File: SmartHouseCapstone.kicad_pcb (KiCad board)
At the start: 2 copper layers, 100.5 x 107.4 mm, 68 parts, among them J1 5V In, J2 3v3 In, J3 1602 LCD, J4 Stepper Motor Terminal, J5 Physical Switch Terminal, J6 MOSFET Switch Module Terminal, J7 Fingerprint Scanner Terminal, J8 Servo Terminal, J9 RFID Module Terminal, Q1 FDN340P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

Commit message: revision 1
added pull-down resistor to FDN430P MosFET Gate

revised pcb layout
revised schematic layout

generated new BOM
generated new Backup
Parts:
- added R27: 2.2k, Resistor_THT:R_Axial_DIN0207_L6.3mm_D2.5mm_P7.62mm_Horizontal, F.Cu at (134.0, 112.0)
- R25: value 47 -> 100
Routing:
- net /Security System/servo_switch: track 61.5 -> 69.6 mm
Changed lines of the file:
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@@
 	)
 	(paper "A4")
+	(title_block
+		(title "Smart House Control Board")
+		(date "2025-11-03")
+		(rev "1")
+	)
 	(layers
 		(0 "F.Cu" signal)
@@
 			)
 		)
-		(property "Value" "47"
+		(property "Value" "100"
 			(at -3.015 0 0)
 			(layer "F.Fab")
@@
 	(footprint "Resistor_THT:R_Axial_DIN0207_L6.3mm_D2.5mm_P7.62mm_Horizontal"
 		(layer "F.Cu")
+		(at 134 112 90)
+		(descr "Resistor, Axial_DIN0207 series, Axial, Horizontal, pin pitch=7.62mm, 0.25W = 1/4W, length*diameter=6.3*2.5mm^2, http://cdn-reichelt.de/documents/datenblatt/B400/1_4W%23YAG.pdf")
+		(tags "Resistor Axial_DIN0207 series Axial Horizontal pin pitch 7.62mm 0.25W = 1/4W length 6.3mm diameter 2.5mm")
+		(property "Reference" "R27"
+			(at 3.81 -2.37 90)
+			(layer "F.SilkS")
+			(effects
+				(font
+					(size 1 1)
+					(thickness 0.15)
+				)
+			)
+		)
+		(property "Value" "2.2k"
+			(at 3.81 2.37 90)
+			(layer "F.Fab")
+			(effects
+				(font
+					(size 1 1)
+					(thickness 0.15)
+				)
+			)
+		)
+		(property "Datasheet" "~"
+			(at 0 0 90)
+			(layer "F.Fab")
+			(hide yes)
+			(effects
+				(font
+					(size 1.27 1.27)
+					(thickness 0.15)
+				)
+			)
+		)
+		(property "Description" "Resistor"
+			(at 0 0 90)
+			(layer "F.Fab")
+			(hide yes)
+			(effects
+				(font
+					(size 1.27 1.27)
+					(thickness 0.15)
+				)
+			)
+		)
+		(property ki_fp_filters "R_*")
+		(sheetname "/Security System/")
+		(sheetfile "SecuritySystem.kicad_sch")
+		(attr through_hole)
+		(fp_line
+			(start 7.08 -1.37)
+			(end 7.08 -1.04)
+			(stroke
+				(width 0.12)
+				(type solid)
+			)
+			(layer "F.SilkS")
+		)
+		(fp_line
+			(start 0.54 -1.37)
+			(end 7.08 -1.37)
+			(stroke
+				(width 0.12)
+				(type solid)
+			)
+			(layer "F.SilkS")
+		)
+		(fp_line
+			(start 0.54 -1.04)
+			(end 0.54 -1.37)
+			(stroke
+				(width 0.12)
+				(type solid)
+			)
+			(layer "F.SilkS")
+		)
+		(fp_line
+			(start 0.54 1.04)
+			(end 0.54 1.37)
+			(stroke
+				(width 0.12)
+				(type solid)
+			)
+			(layer "F.SilkS")
+		)
+		(fp_line
+			(start 7.08 1.37)
+			(end 7.08 1.04)
+			(stroke
+				(width 0.12)
+				(type solid)
+			)
+			(layer "F.SilkS")
+		)
+		(fp_line
+			(start 0.54 1.37)
+			(end 7.08 1.37)
+			(stroke
+				(width 0.12)
+				(type solid)
+			)
+			(layer "F.SilkS")
+		)
+		(fp_rect
+			(start -1.05 -1.5)
+			(end 8.67 1.5)
+			(stroke
+				(width 0.05)
+				(type solid)
+			)
+			(fill no)
+			(layer "F.CrtYd")
+		)
+		(fp_line
+			(start 7.62 0)
+			(end 6.96 0)
+			(stroke
+				(width 0.1)
+				(type solid)
+			)
+			(layer "F.Fab")
+		)
+		(fp_line
+			(start 0 0)
+			(end 0.66 0)
+			(stroke
+				(width 0.1)
+				(type solid)
+			)
+			(layer "F.Fab")
+		)
+		(fp_rect
+			(start 0.66 -1.25)
+			(end 6.96 1.25)
+			(stroke
+				(width 0.1)
+				(type solid)
+			)
+			(fill no)
+			(layer "F.Fab")
+		)
+		(fp_text user "${REFERENCE}"
+			(at 3.81 0 90)
+			(layer "F.Fab")
+			(effects
+				(font
+					(size 1 1)
+					(thickness 0.15)
+				)
+			)
+		)
+		(pad "1" thru_hole circle
+			(at 0 0 90)
+			(size 1.6 1.6)
+			(drill 0.8)
+			(layers "*.Cu" "*.Mask")
+			(remove_unused_layers no)
+			(net 60 "/Security System/servo_switch")
+			(pintype "passive")
+		)
+		(pad "2" thru_hole circle
+			(at 7.62 0 90)
+			(size 1.6 1.6)
+			(drill 0.8)
+			(layers "*.Cu" "*.Mask")
+			(remove_unused_layers no)
+			(net 1 "GND")
+			(pintype "passive")
+		)
+		(embedded_fonts no)
+		(model "${KICAD9_3DMODEL_DIR}/Resistor_THT.3dshapes/R_Axial_DIN0207_L6.3mm_D2.5mm_P7.62mm_Horizontal.step"
+			(offset
+				(xyz 0 0 0)
+			)
+			(scale
+				(xyz 1 1 1)
+			)
+			(rotate
+				(xyz 0 0 0)
+			)
+		)
+	)
+	(footprint "Resistor_THT:R_Axial_DIN0207_L6.3mm_D2.5mm_P7.62mm_Horizontal"
+		(layer "F.Cu")
 		(at 83.92 92.3 180)
 		(descr "Resistor, Axial_DIN0207 series, Axial, Horizontal, pin pitch=7.62mm, 0.25W = 1/4W, length*diameter=6.3*2.5mm^2, http://cdn-reichelt.de/documents/datenblatt/B400/1_4W%23YAG.pdf")
@@
 	)
 	(segment
+		(start 134.256 120)
+		(end 134.256 112.256)
+		(width 0.8)
+		(layer "B.Cu")
+		(net 60)
+	)
+	(segment
 		(start 132.59 123.48)
 		(end 134.256 121.814)
@@
 	)
 	(segment
-		(start 134.256 121.814)
+		(start 134.256 112.256)
+		(end 134 112)
+		(width 0.8)
+		(layer "B.Cu")
+		(net 60)
+	)
+	(segment
+		(start 134.256 120)
 		(end 134.256 119.596)
 		(width 0.8)
 		(layer "B.Cu")
+		(net 60)
+	)
+	(segment
+		(start 134.256 121.814)
+		(end 134.256 120)
+		(width 0.8)
+		(layer "B.Cu")

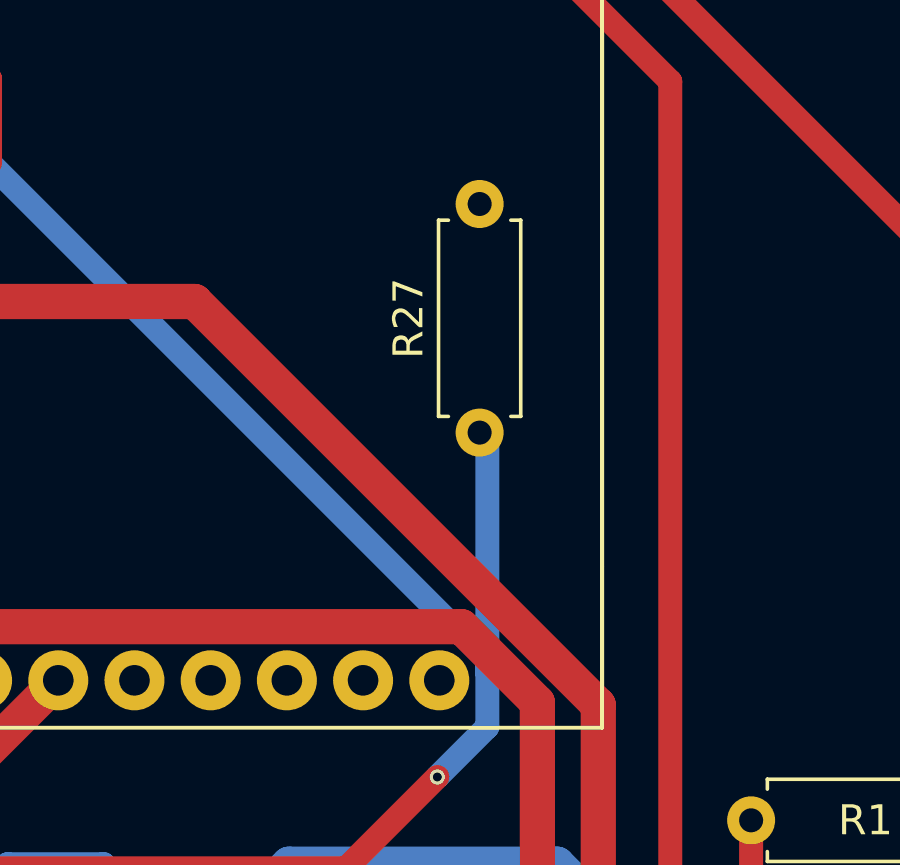
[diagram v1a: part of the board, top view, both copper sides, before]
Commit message: updated gerber files
re-add of resistor footprints -- for some reason it was removed
re-add of the new pull-down resistor R27 -- for some reason it was not
in the schematic but it exists in pcb
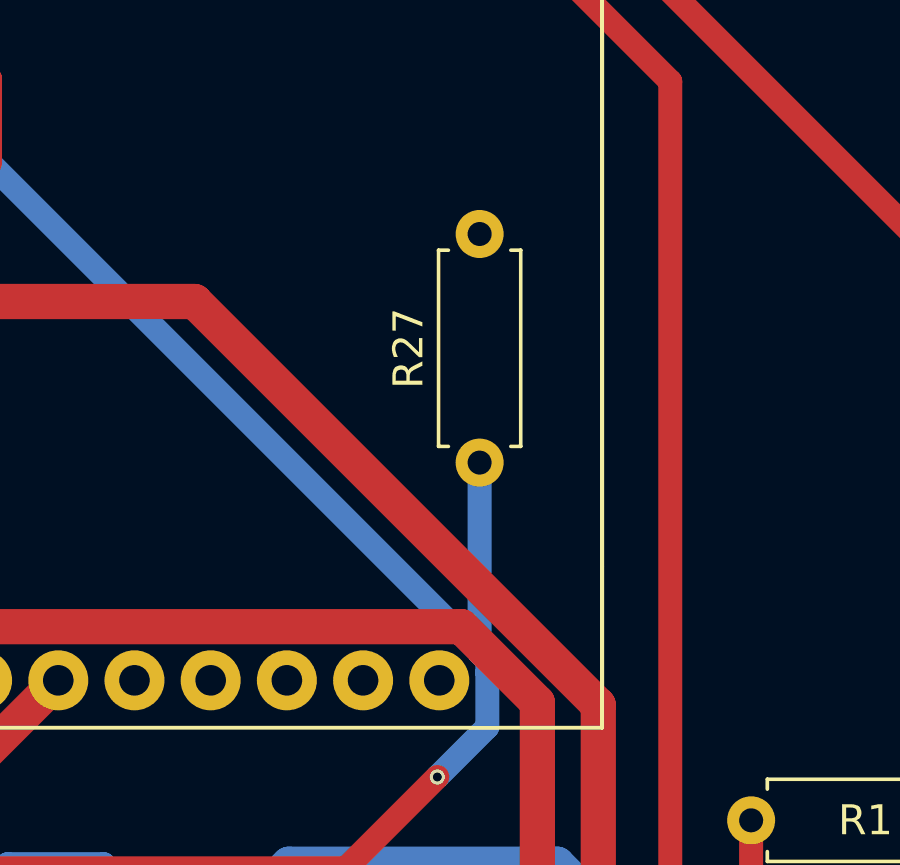
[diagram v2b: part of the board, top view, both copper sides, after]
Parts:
- moved R27 1.00 mm to (134.0, 113.0)
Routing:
- net /Security System/servo_switch: track 69.6 -> 68.2 mm
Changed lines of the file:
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@@
 	(footprint "Resistor_THT:R_Axial_DIN0207_L6.3mm_D2.5mm_P7.62mm_Horizontal"
 		(layer "F.Cu")
+		(at 134 113 90)
+		(descr "Resistor, Axial_DIN0207 series, Axial, Horizontal, pin pitch=7.62mm, 0.25W = 1/4W, length*diameter=6.3*2.5mm^2, http://cdn-reichelt.de/documents/datenblatt/B400/1_4W%23YAG.pdf")
+		(tags "Resistor Axial_DIN0207 series Axial Horizontal pin pitch 7.62mm 0.25W = 1/4W length 6.3mm diameter 2.5mm")
+		(property "Reference" "R27"
+			(at 3.81 -2.37 90)
+			(layer "F.SilkS")
+			(effects
+				(font
+					(size 1 1)
+					(thickness 0.15)
+				)
+			)
+		)
+		(property "Value" "2.2k"
+			(at 3.81 2.37 90)
+			(layer "F.Fab")
+			(effects
+				(font
+					(size 1 1)
+					(thickness 0.15)
+				)
+			)
+		)
+		(property "Datasheet" "~"
+			(at 0 0 90)
+			(layer "F.Fab")
+			(hide yes)
+			(effects
+				(font
+					(size 1.27 1.27)
+					(thickness 0.15)
+				)
+			)
+		)
+		(property "Description" "Resistor"
+			(at 0 0 90)
+			(layer "F.Fab")
+			(hide yes)
+			(effects
+				(font
+					(size 1.27 1.27)
+					(thickness 0.15)
+				)
+			)
+		)
+		(property ki_fp_filters "R_*")
+		(sheetname "/Security System/")
+		(sheetfile "SecuritySystem.kicad_sch")
+		(attr through_hole)
+		(fp_line
+			(start 7.08 -1.37)
+			(end 7.08 -1.04)
+			(stroke
+				(width 0.12)
+				(type solid)
+			)
+			(layer "F.SilkS")
+		)
+		(fp_line
+			(start 0.54 -1.37)
+			(end 7.08 -1.37)
+			(stroke
+				(width 0.12)
+				(type solid)
+			)
+			(layer "F.SilkS")
+		)
+		(fp_line
+			(start 0.54 -1.04)
+			(end 0.54 -1.37)
+			(stroke
+				(width 0.12)
+				(type solid)
+			)
+			(layer "F.SilkS")
+		)
+		(fp_line
+			(start 0.54 1.04)
+			(end 0.54 1.37)
+			(stroke
+				(width 0.12)
+				(type solid)
+			)
+			(layer "F.SilkS")
+		)
+		(fp_line
+			(start 7.08 1.37)
+			(end 7.08 1.04)
+			(stroke
+				(width 0.12)
+				(type solid)
+			)
+			(layer "F.SilkS")
+		)
+		(fp_line
+			(start 0.54 1.37)
+			(end 7.08 1.37)
+			(stroke
+				(width 0.12)
+				(type solid)
+			)
+			(layer "F.SilkS")
+		)
+		(fp_rect
+			(start -1.05 -1.5)
+			(end 8.67 1.5)
+			(stroke
+				(width 0.05)
+				(type solid)
+			)
+			(fill no)
+			(layer "F.CrtYd")
+		)
+		(fp_line
+			(start 7.62 0)
+			(end 6.96 0)
+			(stroke
+				(width 0.1)
+				(type solid)
+			)
+			(layer "F.Fab")
+		)
+		(fp_line
+			(start 0 0)
+			(end 0.66 0)
+			(stroke
+				(width 0.1)
+				(type solid)
+			)
+			(layer "F.Fab")
+		)
+		(fp_rect
+			(start 0.66 -1.25)
+			(end 6.96 1.25)
+			(stroke
+				(width 0.1)
+				(type solid)
+			)
+			(fill no)
+			(layer "F.Fab")
+		)
+		(fp_text user "${REFERENCE}"
+			(at 3.81 0 90)
+			(layer "F.Fab")
+			(effects
+				(font
+					(size 1 1)
+					(thickness 0.15)
+				)
+			)
+		)
+		(pad "1" thru_hole circle
+			(at 0 0 90)
+			(size 1.6 1.6)
+			(drill 0.8)
+			(layers "*.Cu" "*.Mask")
+			(remove_unused_layers no)
+			(net 60 "/Security System/servo_switch")
+			(pintype "passive")
+		)
+		(pad "2" thru_hole circle
+			(at 7.62 0 90)
+			(size 1.6 1.6)
+			(drill 0.8)
+			(layers "*.Cu" "*.Mask")
+			(remove_unused_layers no)
+			(net 1 "GND")
+			(pintype "passive")
+		)
+		(embedded_fonts no)
+		(model "${KICAD9_3DMODEL_DIR}/Resistor_THT.3dshapes/R_Axial_DIN0207_L6.3mm_D2.5mm_P7.62mm_Horizontal.step"
+			(offset
+				(xyz 0 0 0)
+			)
+			(scale
+				(xyz 1 1 1)
+			)
+			(rotate
+				(xyz 0 0 0)
+			)
+		)
+	)
+	(footprint "Resistor_THT:R_Axial_DIN0207_L6.3mm_D2.5mm_P7.62mm_Horizontal"
+		(layer "F.Cu")
 		(at 83.77 114.625 180)
 		(descr "Resistor, Axial_DIN0207 series, Axial, Horizontal, pin pitch=7.62mm, 0.25W = 1/4W, length*diameter=6.3*2.5mm^2, http://cdn-reichelt.de/documents/datenblatt/B400/1_4W%23YAG.pdf")
@@
 	(footprint "Resistor_THT:R_Axial_DIN0207_L6.3mm_D2.5mm_P7.62mm_Horizontal"
 		(layer "F.Cu")
-		(at 134 112 90)
-		(descr "Resistor, Axial_DIN0207 series, Axial, Horizontal, pin pitch=7.62mm, 0.25W = 1/4W, length*diameter=6.3*2.5mm^2, http://cdn-reichelt.de/documents/datenblatt/B400/1_4W%23YAG.pdf")
-		(tags "Resistor Axial_DIN0207 series Axial Horizontal pin pitch 7.62mm 0.25W = 1/4W length 6.3mm diameter 2.5mm")
-		(property "Reference" "R27"
-			(at 3.81 -2.37 90)
-			(layer "F.SilkS")
-			(effects
-				(font
-					(size 1 1)
-					(thickness 0.15)
-				)
-			)
-		)
-		(property "Value" "2.2k"
-			(at 3.81 2.37 90)
-			(layer "F.Fab")
-			(effects
-				(font
-					(size 1 1)
-					(thickness 0.15)
-				)
-			)
-		)
-		(property "Datasheet" "~"
-			(at 0 0 90)
-			(layer "F.Fab")
-			(hide yes)
-			(effects
-				(font
-					(size 1.27 1.27)
-					(thickness 0.15)
-				)
-			)
-		)
-		(property "Description" "Resistor"
-			(at 0 0 90)
-			(layer "F.Fab")
-			(hide yes)
-			(effects
-				(font
-					(size 1.27 1.27)
-					(thickness 0.15)
-				)
-			)
-		)
-		(property ki_fp_filters "R_*")
-		(sheetname "/Security System/")
-		(sheetfile "SecuritySystem.kicad_sch")
-		(attr through_hole)
-		(fp_line
-			(start 7.08 -1.37)
-			(end 7.08 -1.04)
-			(stroke
-				(width 0.12)
-				(type solid)
-			)
-			(layer "F.SilkS")
-		)
-		(fp_line
-			(start 0.54 -1.37)
-			(end 7.08 -1.37)
-			(stroke
-				(width 0.12)
-				(type solid)
-			)
-			(layer "F.SilkS")
-		)
-		(fp_line
-			(start 0.54 -1.04)
-			(end 0.54 -1.37)
-			(stroke
-				(width 0.12)
-				(type solid)
-			)
-			(layer "F.SilkS")
-		)
-		(fp_line
-			(start 0.54 1.04)
-			(end 0.54 1.37)
-			(stroke
-				(width 0.12)
-				(type solid)
-			)
-			(layer "F.SilkS")
-		)
-		(fp_line
-			(start 7.08 1.37)
-			(end 7.08 1.04)
-			(stroke
-				(width 0.12)
-				(type solid)
-			)
-			(layer "F.SilkS")
-		)
-		(fp_line
-			(start 0.54 1.37)
-			(end 7.08 1.37)
-			(stroke
-				(width 0.12)
-				(type solid)
-			)
-			(layer "F.SilkS")
-		)
-		(fp_rect
-			(start -1.05 -1.5)
-			(end 8.67 1.5)
-			(stroke
-				(width 0.05)
-				(type solid)
-			)
-			(fill no)
-			(layer "F.CrtYd")
-		)
-		(fp_line
-			(start 7.62 0)
-			(end 6.96 0)
-			(stroke
-				(width 0.1)
-				(type solid)
-			)
-			(layer "F.Fab")
-		)
-		(fp_line
-			(start 0 0)
-			(end 0.66 0)
-			(stroke
-				(width 0.1)
-				(type solid)
-			)
-			(layer "F.Fab")
-		)
-		(fp_rect
-			(start 0.66 -1.25)
-			(end 6.96 1.25)
-			(stroke
-				(width 0.1)
-				(type solid)
-			)
-			(fill no)
-			(layer "F.Fab")
-		)
-		(fp_text user "${REFERENCE}"
-			(at 3.81 0 90)
-			(layer "F.Fab")
-			(effects
-				(font
-					(size 1 1)
-					(thickness 0.15)
-				)
-			)
-		)
-		(pad "1" thru_hole circle
-			(at 0 0 90)
-			(size 1.6 1.6)
-			(drill 0.8)
-			(layers "*.Cu" "*.Mask")
-			(remove_unused_layers no)
-			(net 60 "/Security System/servo_switch")
-			(pintype "passive")
-		)
-		(pad "2" thru_hole circle
-			(at 7.62 0 90)
-			(size 1.6 1.6)
-			(drill 0.8)
-			(layers "*.Cu" "*.Mask")
-			(remove_unused_layers no)
-			(net 1 "GND")
-			(pintype "passive")
-		)
-		(embedded_fonts no)
-		(model "${KICAD9_3DMODEL_DIR}/Resistor_THT.3dshapes/R_Axial_DIN0207_L6.3mm_D2.5mm_P7.62mm_Horizontal.step"
-			(offset
-				(xyz 0 0 0)
-			)
-			(scale
-				(xyz 1 1 1)
-			)
-			(rotate
-				(xyz 0 0 0)
-			)
-		)
-	)
-	(footprint "Resistor_THT:R_Axial_DIN0207_L6.3mm_D2.5mm_P7.62mm_Horizontal"
-		(layer "F.Cu")
 		(at 83.92 92.3 180)
 		(descr "Resistor, Axial_DIN0207 series, Axial, Horizontal, pin pitch=7.62mm, 0.25W = 1/4W, length*diameter=6.3*2.5mm^2, http://cdn-reichelt.de/documents/datenblatt/B400/1_4W%23YAG.pdf")
@@
 	)
 	(segment
-		(start 134.256 120)
-		(end 134.256 112.256)
+		(start 132.59 123.48)
+		(end 134.256 121.814)
 		(width 0.8)
 		(layer "B.Cu")
@@
 	)
 	(segment
-		(start 132.59 123.48)
-		(end 134.256 121.814)
+		(start 134.256 119.596)
+		(end 134 119.34)
 		(width 0.8)
 		(layer "B.Cu")
@@
 	)
 	(segment
-		(start 134.256 112.256)
-		(end 134 112)
+		(start 134.256 121.814)
+		(end 134.256 120)
 		(width 0.8)
 		(layer "B.Cu")
@@
 	)
 	(segment
-		(start 134.256 121.814)
-		(end 134.256 120)
+		(start 134 119.34)
+		(end 134 113)
 		(width 0.8)
 		(layer "B.Cu")

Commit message: revision 2
modified pull-up/pull-down resistor values
modified switch1/switch2 input voltage from 5V to 3v3

added proper sheet detail (designer, cc license)
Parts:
- R10, R11, R12, R13, R14, R15, R16, R7, R8, R9: value 1k -> 10k
- R27: value 2.2k -> 10k
- moved R7 7.66 mm to (114.0, 45.8), turned to -90 degrees
- moved R10 7.62 mm to (110.7, 53.4), turned to 90 degrees
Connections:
- C18 pad 2: /Power Distribution/3v3 -> /Lighting Control System/3v3
- C19 pad 2: /Power Distribution/3v3 -> /Lighting Control System/3v3
- C2 pad 1: /Power Distribution/3v3 -> /Lighting Control System/3v3
- D2 pad 1: /Power Distribution/3v3 -> /Lighting Control System/3v3
- J9 pad 2: /Power Distribution/3v3 -> /Lighting Control System/3v3
- R10 pad 1: /Lighting Control System/switch_2 -> /Lighting Control System/3v3
- R10 pad 2: /Automatic Garage Door/5V -> /Lighting Control System/switch_2
- R7 pad 1: /Automatic Garage Door/5V -> /Lighting Control System/switch_1
- R7 pad 2: /Lighting Control System/switch_1 -> /Lighting Control System/3v3
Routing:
- net /Lighting Control System/3v3: track 0.00 -> 205.0 mm
- net /Power Distribution/3v3: track 151.0 -> 0.00 mm
- net /Automatic Garage Door/5V: track 328.7 -> 308.7 mm
